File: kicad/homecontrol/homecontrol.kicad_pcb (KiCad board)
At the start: 2 copper layers, 103 x 86.5 mm, 71 parts, among them J1 Screw_Terminal_01x09, J2 Screw_Terminal_01x09, J3 Screw_Terminal_01x09, J4 Screw_Terminal_01x09, J5 AVR-ISP-10, U1 ATmega48P-20PU, U2 L7805ABP, U3 ULN2803A, U4 MAX232EEPE+, U5 A817, U6 A817

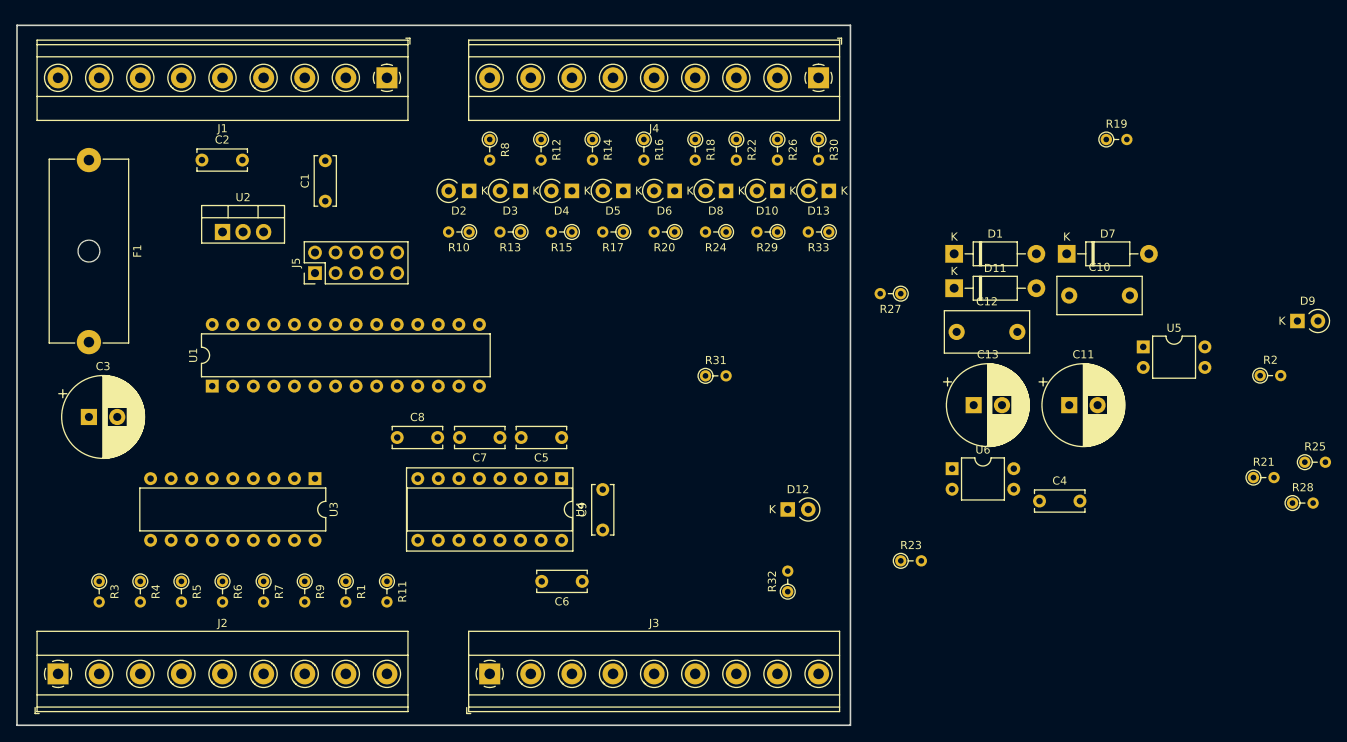
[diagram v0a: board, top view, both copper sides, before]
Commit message: Updated footprints and BOM
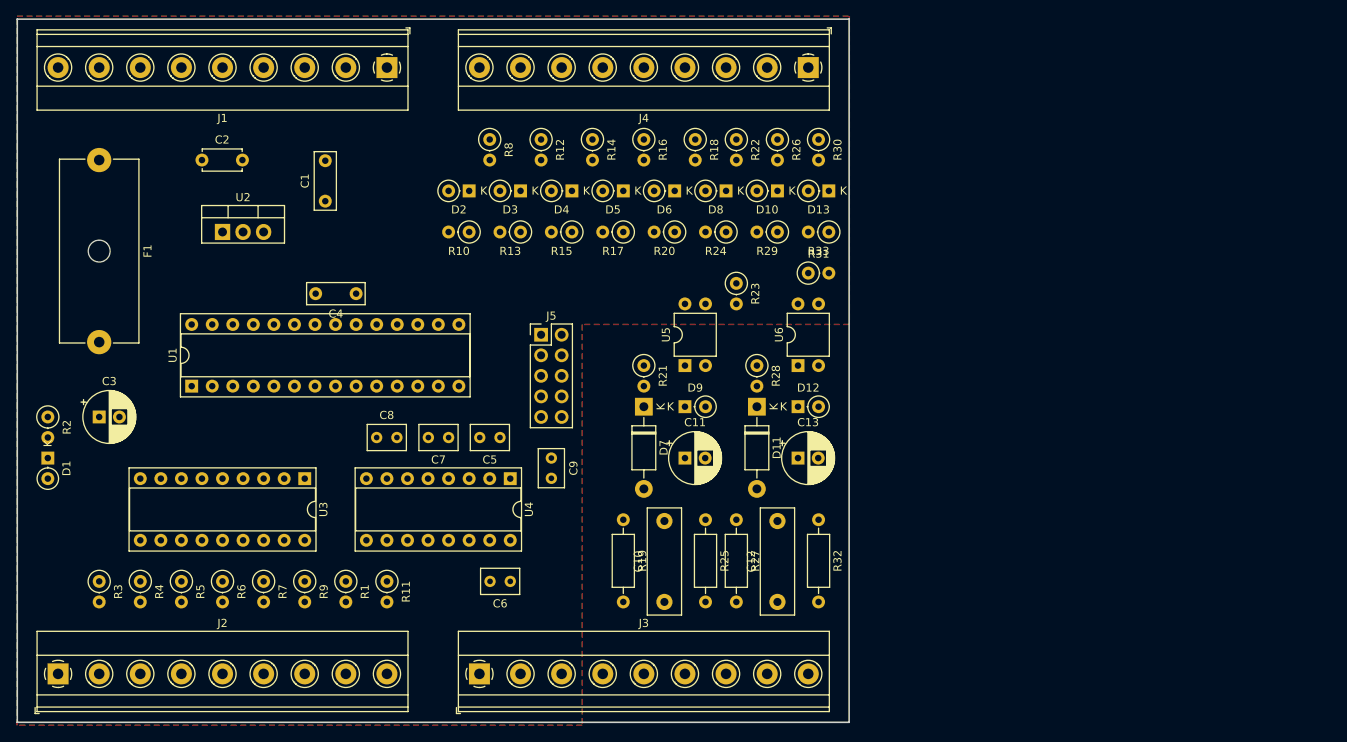
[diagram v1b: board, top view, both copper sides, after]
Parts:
- C1, C4: footprint Capacitor_THT:C_Disc_D6.0mm_W2.5mm_P5.00mm -> Capacitor_THT:C_Rect_L7.0mm_W2.5mm_P5.00mm
- C10: footprint Capacitor_THT:C_Rect_L10.3mm_W4.5mm_P7.50mm_MKS4 -> Capacitor_THT:C_Rect_L13.0mm_W4.0mm_P10.00mm_FKS3_FKP3_MKS4
- C11, C13, C3: footprint Capacitor_THT:CP_Radial_D10.0mm_P3.50mm -> Capacitor_THT:CP_Radial_D6.3mm_P2.50mm
- C12: footprint Capacitor_THT:C_Rect_L10.3mm_W5.0mm_P7.50mm_MKS4 -> Capacitor_THT:C_Rect_L13.0mm_W4.0mm_P10.00mm_FKS3_FKP3_MKS4
- C2: footprint Capacitor_THT:C_Disc_D6.0mm_W2.5mm_P5.00mm -> Capacitor_THT:C_Disc_D4.7mm_W2.5mm_P5.00mm
- C5, C6, C7, C8, C9: footprint Capacitor_THT:C_Disc_D6.0mm_W2.5mm_P5.00mm -> Capacitor_THT:C_Rect_L4.6mm_W3.0mm_P2.50mm_MKS02_FKP02
- D1: footprint Diode_THT:D_DO-41_SOD81_P10.16mm_Horizontal -> Diode_THT:D_DO-35_SOD27_P2.54mm_Vertical_KathodeUp
- D10, D12, D13, D2, D3, D4, D5, D6, D8, D9: footprint Diode_THT:D_A-405_P2.54mm_Vertical_KathodeUp -> Diode_THT:D_DO-35_SOD27_P2.54mm_Vertical_KathodeUp
- R1, R10, R11, R12, R13, R14, R15, R16, R17, R18, R2, R20, R21, R22, R23, R24, R26, R28, R29, R3, R30, R31, R33, R4, R5, R6, R7, R8, R9: footprint Resistor_THT:R_Axial_DIN0204_L3.6mm_D1.6mm_P2.54mm_Vertical -> Resistor_THT:R_Axial_DIN0207_L6.3mm_D2.5mm_P2.54mm_Vertical
- R19, R27: footprint Resistor_THT:R_Axial_DIN0204_L3.6mm_D1.6mm_P2.54mm_Vertical -> Resistor_THT:R_Axial_DIN0207_L6.3mm_D2.5mm_P10.16mm_Horizontal
- R25, R32: value 100k -> 100; footprint Resistor_THT:R_Axial_DIN0204_L3.6mm_D1.6mm_P2.54mm_Vertical -> Resistor_THT:R_Axial_DIN0207_L6.3mm_D2.5mm_P10.16mm_Horizontal
- U1: footprint Package_DIP:DIP-28_W7.62mm -> Package_DIP:DIP-28_W7.62mm_Socket
- U3: footprint Package_DIP:DIP-18_W7.62mm -> Package_DIP:DIP-18_W7.62mm_Socket
- moved R2 149.9 mm to (102.9, 111.8), turned to 270 degrees
- moved D1 114.8 mm to (102.9, 116.8), turned to 270 degrees
- moved C4 88.3 mm to (141.0, 96.5), turned to 180 degrees
- moved R21 76.6 mm to (176.5, 105.4), turned to 270 degrees
- moved D9 76.4 mm to (181.6, 110.5)
- moved R19 76.0 mm to (174.0, 124.5), turned to 270 degrees
- moved R25 74.4 mm to (184.2, 124.5), turned to 270 degrees
- moved R28 68.3 mm to (190.5, 105.4), turned to 270 degrees
- moved C10 62.7 mm to (179.1, 134.6), turned to 90 degrees
- moved U5 56.7 mm to (181.6, 105.4), turned to 90 degrees
- moved D7 55.6 mm to (176.5, 110.5), turned to 270 degrees
- moved C11 47.9 mm to (181.6, 116.8)
- moved C12 40.0 mm to (193.0, 134.6), turned to 90 degrees
- moved R23 39.9 mm to (188.0, 95.2), turned to 270 degrees
- moved R27 34.5 mm to (188.0, 124.5), turned to 270 degrees
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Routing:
- added copper zone on F.Cu, net GND
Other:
- board size 103 x 86.5 mm -> 102.8 x 86.9 mm

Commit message: First full PCB layout of HomeControl
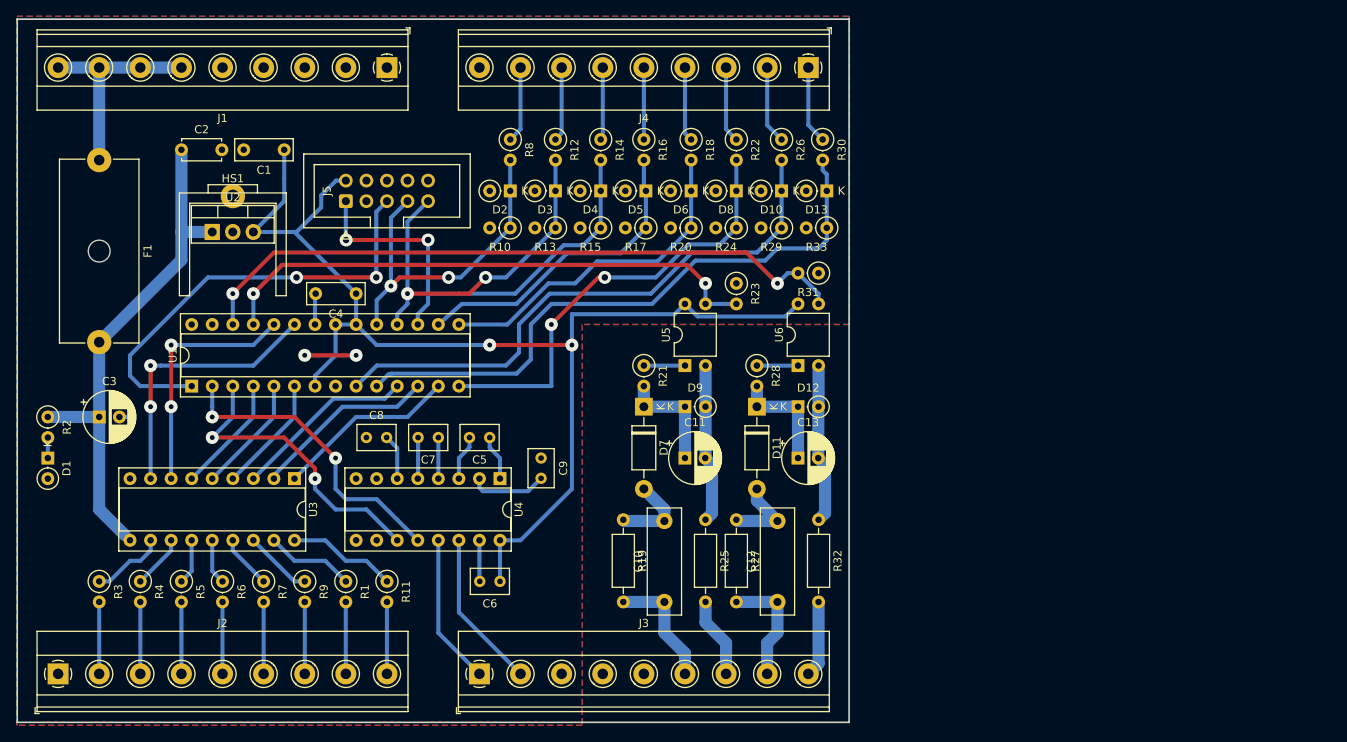
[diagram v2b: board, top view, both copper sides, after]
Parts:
- added HS1: Heatsink_Pad, Custom_Library:Heatsink_Aavid_TO-220_H12.7mm, F.Cu at (125.7, 85.3)
- J5: footprint Connector_PinHeader_2.54mm:PinHeader_2x05_P2.54mm_Vertical -> Connector_IDC:IDC-Header_2x05_P2.54mm_Vertical
- moved J5 29.2 mm to (139.7, 85.1), turned to 90 degrees
- moved C1 8.13 mm to (132.1, 78.7), turned to 180 degrees
- moved R10 5.11 mm to (160.0, 88.4)
- moved D2 5.08 mm to (160.0, 83.8)
- moved R13 4.35 mm to (165.6, 88.4)
- moved D3 4.32 mm to (165.6, 83.8)
- moved R15 3.59 mm to (171.2, 88.4)
- moved D4 3.56 mm to (171.2, 83.8)
- moved C2 2.84 mm to (119.4, 78.7)
- moved R17 2.84 mm to (176.8, 88.4)
- moved D5 2.79 mm to (176.8, 83.8)
- moved R8 2.54 mm to (160.0, 77.5)
- moved R20 2.09 mm to (182.4, 88.4)
- moved D6 2.03 mm to (182.4, 83.8)
- moved R12 1.78 mm to (165.6, 77.5)
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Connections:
- D10 pad 1: DI6 -> DI7
- D13 pad 1: DI7 -> DI8
- D2 pad 1: DI0 -> SCK
- D3 pad 1: DI1 -> MISO
- D4 pad 1: DI2 -> MOSI
- D5 pad 1: MOSI -> DI4
- D6 pad 1: MISO -> DI5
- D8 pad 1: SCK -> DI6
- R10 pad 1: DI0 -> SCK
- R12 pad 2: DI1 -> MISO
- R13 pad 1: DI1 -> MISO
- R14 pad 2: DI2 -> MOSI
- R15 pad 1: DI2 -> MOSI
- R16 pad 2: MOSI -> DI4
- R17 pad 1: MOSI -> DI4
- R18 pad 2: MISO -> DI5
- R20 pad 1: MISO -> DI5
- R22 pad 2: SCK -> DI6
- R24 pad 1: SCK -> DI6
- R26 pad 2: DI6 -> DI7
- R29 pad 1: DI6 -> DI7
- R30 pad 2: DI7 -> DI8
- R33 pad 1: DI7 -> DI8
- R8 pad 2: DI0 -> SCK
- U1 pad 10: DI7 -> DI8
- U1 pad 11: Net-(U1-Pad11) -> DO3
- U1 pad 12: Net-(U1-Pad12) -> DO2
- U1 pad 13: Net-(U1-Pad13) -> DO1
- U1 pad 14: DI0 -> DI6
- U1 pad 15: DI1 -> DI5
- U1 pad 16: DI2 -> DI4
- U1 pad 23: DO0 -> DO8
- U1 pad 24: DO1 -> DO7
- U1 pad 4: Net-(U1-Pad4) -> DO6
- U1 pad 5: Net-(U1-Pad5) -> DO5
- U1 pad 6: Net-(U1-Pad6) -> DO4
- U1 pad 9: DI6 -> DI7
- U3 pad 1: DO0 -> DO1
- U3 pad 2: DO1 -> DO2
- U3 pad 3: Net-(U1-Pad4) -> DO3
- U3 pad 4: Net-(U1-Pad5) -> DO4
- U3 pad 5: Net-(U1-Pad6) -> DO5
- U3 pad 6: Net-(U1-Pad11) -> DO6
- U3 pad 7: Net-(U1-Pad12) -> DO7
- U3 pad 8: Net-(U1-Pad13) -> DO8
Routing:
- net +5V: track 0.00 -> 148.1 mm, vias 0 -> 2
- net S2: track 0.00 -> 82.7 mm, vias 0 -> 2
- net DI8: track 0.00 -> 75.7 mm
- net DI7: track 0.00 -> 71.1 mm
- net S1: track 0.00 -> 68.5 mm, vias 0 -> 2
- net +24V: track 0.00 -> 68.0 mm
- net MOSI: track 0.00 -> 59.0 mm, vias 0 -> 2
- net DI6: track 0.00 -> 55.9 mm, vias 0 -> 2
- net RST: track 0.00 -> 55.1 mm, vias 0 -> 2
- net MISO: track 0.00 -> 47.2 mm, vias 0 -> 2
- net SCK: track 0.00 -> 42.9 mm, vias 0 -> 2
- net DI5: track 0.00 -> 42.0 mm
- net DI4: track 0.00 -> 39.0 mm
- net RXD: track 0.00 -> 37.8 mm, vias 0 -> 2
- net TXD: track 0.00 -> 37.0 mm, vias 0 -> 2
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- added copper zone on B.Cu, net GND
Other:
- net class Default: clearance 0.2 -> 0.5; trace_width 0.25 -> 0.5; via_dia 0.8 -> 1.6; via_drill 0.4 -> 0.8
- net class Power added: clearance 0.9, trace_width 1.5, via_dia 1.6, via_drill 0.8
- net class Power DC added: clearance 0.6, trace_width 1.5, via_dia 1.6, via_drill 0.8
- rule trace_clearance: 0.2 -> 0.5
- rule trace_min: 0.2 -> 0.5
- rule via_min_size: 0.4 -> 1.4

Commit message: Updated HomeControl PCB to KiCAD 7.0, fixed MKS4 footprint
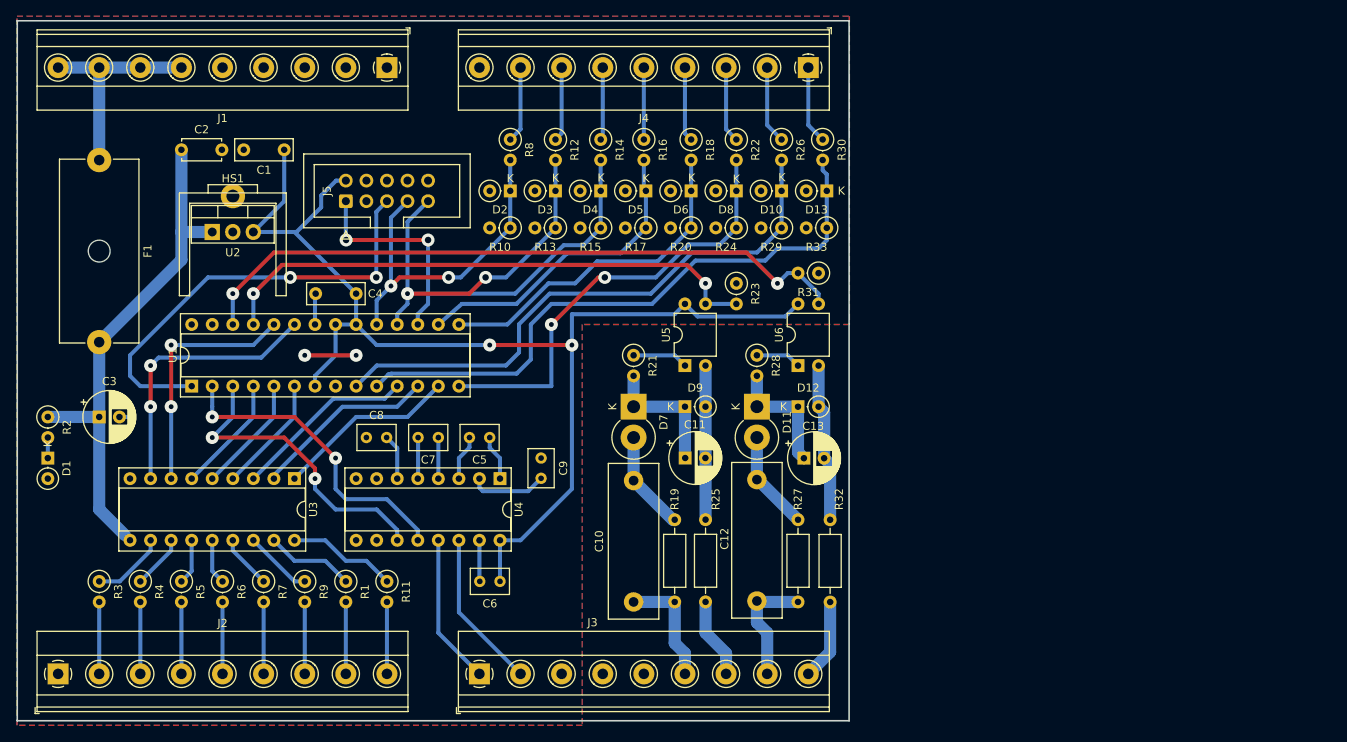
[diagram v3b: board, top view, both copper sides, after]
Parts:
- C10, C12: footprint Capacitor_THT:C_Rect_L13.0mm_W4.0mm_P10.00mm_FKS3_FKP3_MKS4 -> Capacitor_THT:C_Rect_L19.0mm_W6.0mm_P15.00mm_MKS4
- D11, D7: footprint Diode_THT:D_DO-41_SOD81_P10.16mm_Horizontal -> Diode_THT:D_DO-201AD_P3.81mm_Vertical_KathodeUp
- moved R27 7.62 mm to (195.6, 124.5)
- moved R19 6.35 mm to (180.3, 124.5)
- moved C10 3.81 mm to (175.3, 134.6)
- moved C12 2.54 mm to (190.5, 134.5)
- moved R21 1.80 mm to (175.3, 104.1)
- moved R32 1.43 mm to (199.5, 124.5)
- moved D7 1.27 mm to (175.3, 110.5)
- moved R28 1.27 mm to (190.5, 104.1)
- moved C13 0.73 mm to (196.3, 116.9)
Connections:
- net Net-(C10-Pad2) renamed /L11
- net Net-(C11-Pad1) renamed /L12
- net Net-(C11-Pad2) renamed /N11
- net Net-(C12-Pad2) renamed /L21
- net Net-(C13-Pad1) renamed /L22
- net Net-(C13-Pad2) renamed /N21
- net Net-(F1-Pad1) renamed /F1
- HS1 pad 1: (no net) -> unconnected-(HS1-Pad1)
- J1 pad 1: (no net) -> unconnected-(J1-Pin_1-Pad1)
- J2 pad 1: (no net) -> unconnected-(J2-Pin_1-Pad1)
- J3 pad 3: (no net) -> unconnected-(J3-Pin_3-Pad3)
- J3 pad 4: (no net) -> unconnected-(J3-Pin_4-Pad4)
- J3 pad 5: (no net) -> unconnected-(J3-Pin_5-Pad5)
- J4 pad 9: (no net) -> unconnected-(J4-Pin_9-Pad9)
- J5 pad 3: (no net) -> unconnected-(J5-NC-Pad3)
- U1 pad 27: (no net) -> SDA
- U1 pad 28: (no net) -> SCL
- U4 pad 7: (no net) -> unconnected-(U4-T2OUT-Pad7)
- U4 pad 9: (no net) -> unconnected-(U4-R2OUT-Pad9)
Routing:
- net /L12: track 13.9 -> 16.5 mm
- net /L11: track 10.2 -> 12.4 mm
- net /L21: track 10.2 -> 12.3 mm
- net Net-(R21-Pad1): track 5.08 -> 6.88 mm
- net /L22: track 13.9 -> 15.6 mm
- net Net-(J4-Pin_1): track 10.9 -> 9.63 mm
- net RXD: track 37.8 -> 38.5 mm
- net TXD: track 37.0 -> 37.8 mm
- net /N11: track 19.7 -> 19.0 mm
- net DI6: track 55.9 -> 55.2 mm
- net N2: track 9.42 -> 10.00 mm
- net Net-(R28-Pad1): track 5.08 -> 5.61 mm
- net L1: track 15.0 -> 14.5 mm
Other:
- board size 102.8 x 86.9 mm -> 102.8 x 86.5 mm
- net class Default removed
- net class Power removed
- net class Power DC removed
